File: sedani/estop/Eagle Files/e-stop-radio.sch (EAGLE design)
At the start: 33 parts, among them J1 E-STOP HEADER, J2 AVR_SPI_PROG_3X2PTH, J3 Buttons, U1 RFM69HCW, U2 TPS62203DBVR, U3 CD40109BPWRPW16-L, X1 8 MHz

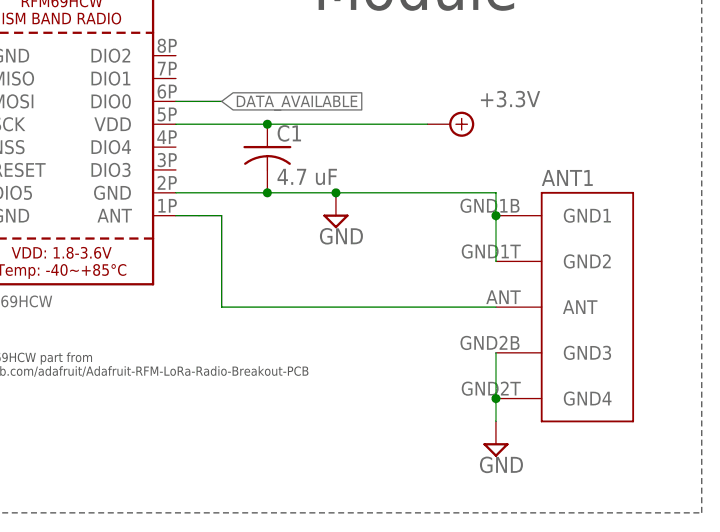
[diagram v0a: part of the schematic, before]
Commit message: changed antenna part
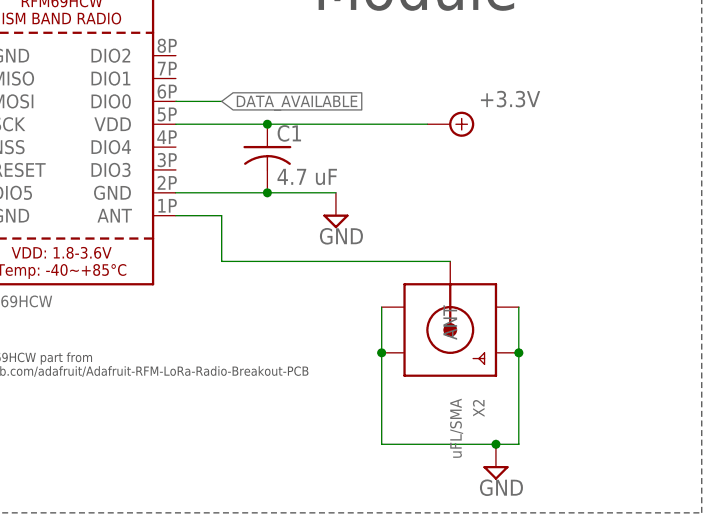
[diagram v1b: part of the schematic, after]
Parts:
- removed ANT1: (no value), estop-v1.0:CON-SMA-EDGE-S
- added X2: uFL/SMA, microbuilder:SMACONNECTOR_EDGE_UFL
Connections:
- net GND: now also X2.GND1, X2.GND2, X2.GND3, X2.GND4; no longer ANT1.GND1, ANT1.GND2, ANT1.GND3, ANT1.GND4
- net RF_SIGNAL: now also X2.ANT; no longer ANT1.ANT
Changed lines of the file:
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@@
 <part name="C5" library="rcl" library_urn="urn:adsk.eagle:library:334" deviceset="C-US" device="C0603" package3d_urn="urn:adsk.eagle:package:23616/2" value="4.7uF"/>
 <part name="C7" library="rcl" library_urn="urn:adsk.eagle:library:334" deviceset="CPOL-US" device="E2.5-7" package3d_urn="urn:adsk.eagle:package:23345/1" value="220uF"/>
-<part name="ANT1" library="estop-v1.0" deviceset="CON-SMA-EDGE-S" device=""/>
 <part name="SUPPLY20" library="supply2" library_urn="urn:adsk.eagle:library:372" deviceset="GND" device=""/>
+<part name="X2" library="microbuilder" deviceset="SMACONNECTOR" device="_EDGE_UFL" value="uFL/SMA"/>
 </parts>
 <sheets>
@@
 <attribute name="VALUE" x="255.016" y="-27.051" size="1.778" layer="96"/>
 </instance>
-<instance part="ANT1" gate="G$1" x="358.14" y="-30.48" smashed="yes">
-<attribute name="VALUE" x="358.14" y="-45.72" size="1.778" layer="95" font="vector"/>
-<attribute name="NAME" x="358.14" y="-15.24" size="1.778" layer="95" font="vector" align="top-left"/>
-</instance>
-<instance part="SUPPLY20" gate="GND" x="353.06" y="-45.72" smashed="yes">
-<attribute name="VALUE" x="351.155" y="-48.895" size="1.778" layer="96"/>
+<instance part="SUPPLY20" gate="GND" x="353.06" y="-48.26" smashed="yes">
+<attribute name="VALUE" x="351.155" y="-51.435" size="1.778" layer="96"/>
+</instance>
+<instance part="X2" gate="G$1" x="347.98" y="-33.02" smashed="yes" rot="R270">
+<attribute name="NAME" x="350.52" y="-40.64" size="1.27" layer="95" rot="R270"/>
+<attribute name="VALUE" x="347.98" y="-40.64" size="1.27" layer="95" rot="R270"/>
 </instance>
 </instances>
@@
 <wire x1="327.66" y1="-17.78" x2="335.28" y2="-17.78" width="0.1524" layer="91"/>
 <junction x="327.66" y="-17.78"/>
-<wire x1="335.28" y1="-17.78" x2="353.06" y2="-17.78" width="0.1524" layer="91"/>
-<junction x="335.28" y="-17.78"/>
-<pinref part="ANT1" gate="G$1" pin="GND2"/>
-<wire x1="353.06" y1="-17.78" x2="353.06" y2="-20.32" width="0.1524" layer="91"/>
-<pinref part="ANT1" gate="G$1" pin="GND1"/>
-<wire x1="353.06" y1="-20.32" x2="353.06" y2="-25.4" width="0.1524" layer="91"/>
-<junction x="353.06" y="-20.32"/>
 </segment>
 <segment>
@@
 </segment>
 <segment>
+<pinref part="X2" gate="G$1" pin="GND1"/>
+<pinref part="X2" gate="G$1" pin="GND2"/>
+<wire x1="355.6" y1="-30.48" x2="355.6" y2="-35.56" width="0.1524" layer="91"/>
 <pinref part="SUPPLY20" gate="GND" pin="GND"/>
-<pinref part="ANT1" gate="G$1" pin="GND4"/>
-<wire x1="353.06" y1="-43.18" x2="353.06" y2="-40.64" width="0.1524" layer="91"/>
-<pinref part="ANT1" gate="G$1" pin="GND3"/>
-<wire x1="353.06" y1="-40.64" x2="353.06" y2="-35.56" width="0.1524" layer="91"/>
-<junction x="353.06" y="-40.64"/>
+<wire x1="355.6" y1="-35.56" x2="355.6" y2="-45.72" width="0.1524" layer="91"/>
+<wire x1="355.6" y1="-45.72" x2="353.06" y2="-45.72" width="0.1524" layer="91"/>
+<junction x="355.6" y="-35.56"/>
+<pinref part="X2" gate="G$1" pin="GND3"/>
+<pinref part="X2" gate="G$1" pin="GND4"/>
+<wire x1="340.36" y1="-30.48" x2="340.36" y2="-35.56" width="0.1524" layer="91"/>
+<wire x1="340.36" y1="-35.56" x2="340.36" y2="-45.72" width="0.1524" layer="91"/>
+<wire x1="340.36" y1="-45.72" x2="353.06" y2="-45.72" width="0.1524" layer="91"/>
+<junction x="340.36" y="-35.56"/>
+<junction x="353.06" y="-45.72"/>
 </segment>
 </net>
@@
 <net name="RF_SIGNAL" class="2">
 <segment>
-<pinref part="ANT1" gate="G$1" pin="ANT"/>
-<wire x1="322.58" y1="-30.48" x2="353.06" y2="-30.48" width="0.1524" layer="91"/>
 <pinref part="U1" gate="G$1" pin="ANT"/>
-<wire x1="317.5" y1="-20.32" x2="320.04" y2="-20.32" width="0.1524" layer="91"/>
-<wire x1="322.58" y1="-30.48" x2="322.58" y2="-20.32" width="0.1524" layer="91"/>
-<wire x1="322.58" y1="-20.32" x2="320.04" y2="-20.32" width="0.1524" layer="91"/>
-</segment>
-</net>
+<wire x1="322.58" y1="-20.32" x2="317.5" y2="-20.32" width="0.1524" layer="91"/>
+<pinref part="X2" gate="G$1" pin="ANT"/>
+<wire x1="347.98" y1="-25.4" x2="322.58" y2="-25.4" width="0.1524" layer="91"/>
+<wire x1="322.58" y1="-25.4" x2="322.58" y2="-20.32" width="0.1524" layer="91"/>
+</segment>
+</net>

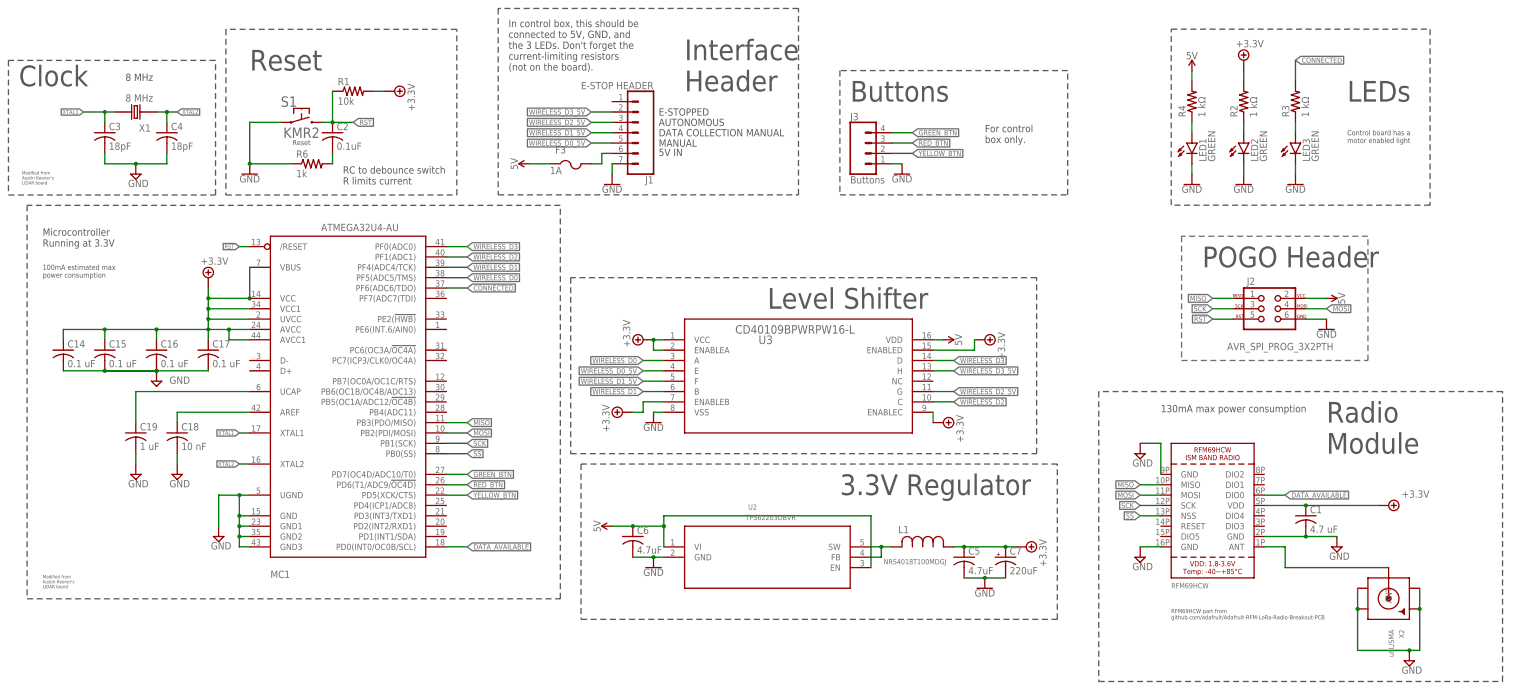
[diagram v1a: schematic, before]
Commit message: fixed library parts and generated board
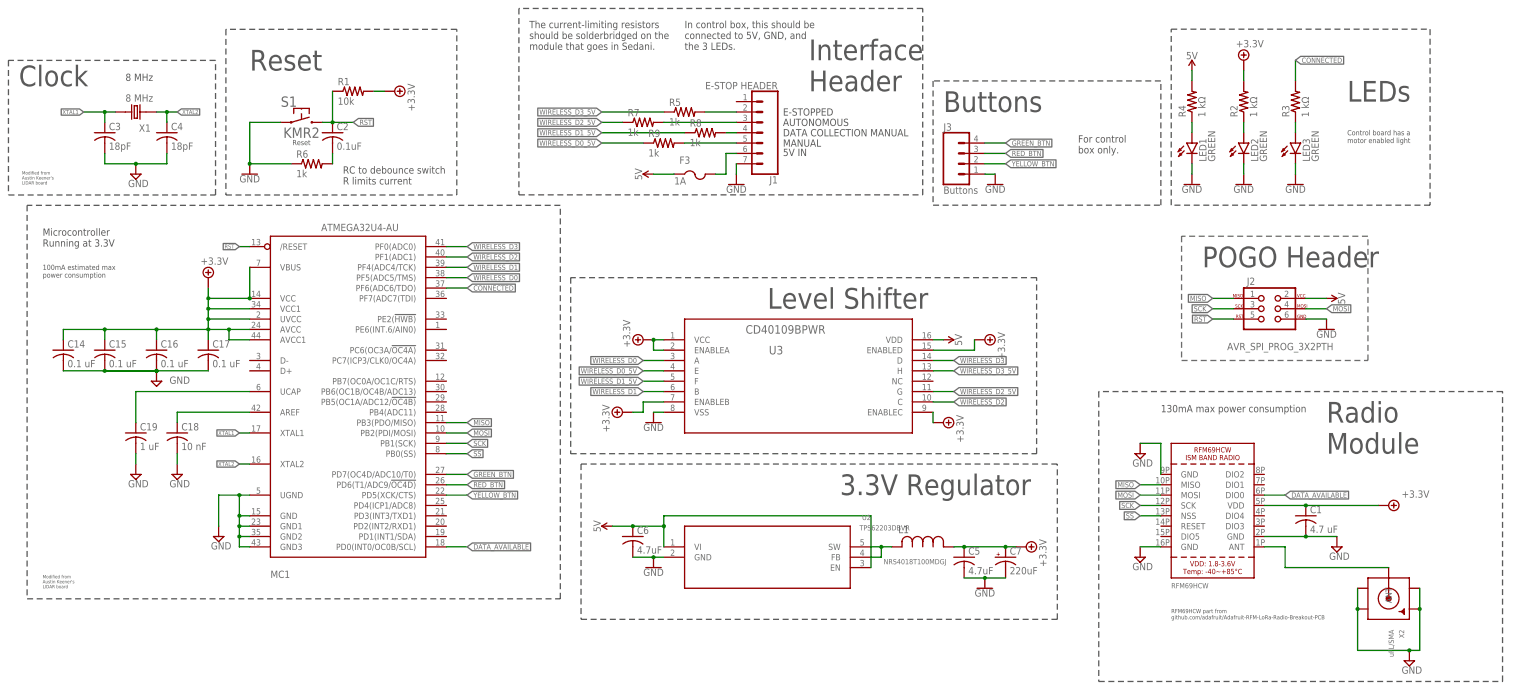
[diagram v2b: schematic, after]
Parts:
- added R5, R7, R8, R9: 1k, rcl:R-US_R0603
- U3: value CD40109BPWRPW16-L -> CD40109BPWR; device estop-v1.0:CD40109BPWRPW16-L -> estop-v1.0:CD40109BPWR
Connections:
- new net N$10: J1.3, R7.2
- new net N$6: J1.4, R8.2
- new net N$8: J1.5, R9.2
- new net N$9: J1.2, R5.2
- net WIRELESS_D0_5V: now also R9.1; no longer J1.5
- net WIRELESS_D1_5V: now also R8.1; no longer J1.4
- net WIRELESS_D2_5V: now also R7.1; no longer J1.3
- net WIRELESS_D3_5V: now also R5.1; no longer J1.2
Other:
- note added: "In control box, this should be connected to 5V, GND, and the 3 LEDs."
- note added: "The current-limiting resistors should be solderbridged on the module that goes in Sedani."
- note removed: "In control box, this should be connected to 5V, GND, and the 3 LEDs. Don't forget the current-limiting resistors (not on the board)."
- moved on the sheet: F3, J1, J3

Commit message: major parts on board
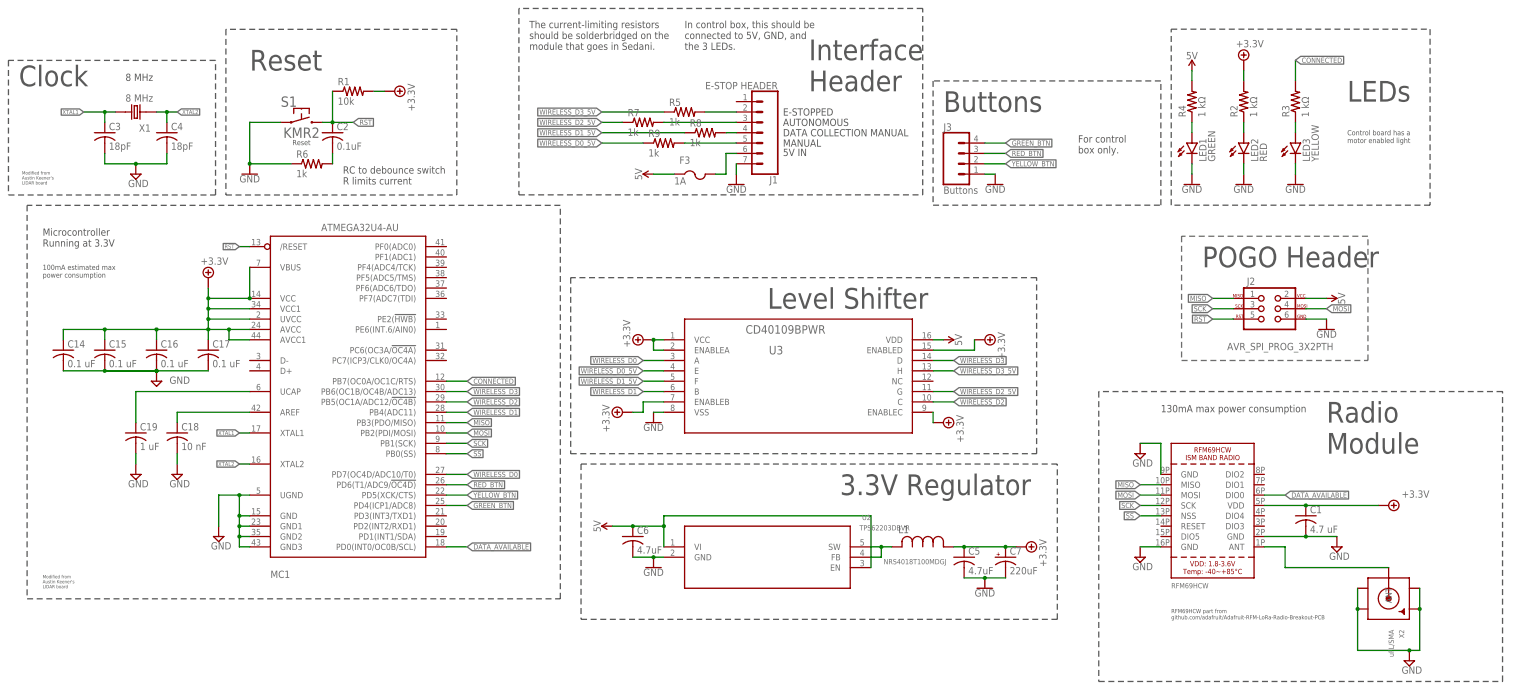
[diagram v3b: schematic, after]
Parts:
- LED2: value GREEN -> RED
- LED3: value GREEN -> YELLOW
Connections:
- net CONNECTED: now also MC1.PB7(OC0A/OC1C/RTS); no longer MC1.PF6(ADC6/TDO)
- net GREEN_BTN: now also MC1.PD4(ICP1/ADC8); no longer MC1.PD7(OC4D/ADC10/T0)
- net WIRELESS_D0: now also MC1.PD7(OC4D/ADC10/T0); no longer MC1.PF5(ADC5/TMS)
- net WIRELESS_D1: now also MC1.PB4(ADC11); no longer MC1.PF4(ADC4/TCK)
- net WIRELESS_D2: now also MC1.PB5(OC1A/ADC12/!OC4B); no longer MC1.PF1(ADC1)
- net WIRELESS_D3: now also MC1.PB6(OC1B/OC4B/ADC13); no longer MC1.PF0(ADC0)
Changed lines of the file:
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@@
 <part name="R4" library="rcl" library_urn="urn:adsk.eagle:library:334" deviceset="R-US_" device="R0603" package3d_urn="urn:adsk.eagle:package:23555/3" value="1 kΩ"/>
 <part name="GND5" library="SparkFun-PowerSymbols" deviceset="GND" device=""/>
-<part name="LED2" library="led" library_urn="urn:adsk.eagle:library:259" deviceset="LED" device="CHIP-LED0603" package3d_urn="urn:adsk.eagle:package:15819/3" value="GREEN"/>
+<part name="LED2" library="led" library_urn="urn:adsk.eagle:library:259" deviceset="LED" device="CHIP-LED0603" package3d_urn="urn:adsk.eagle:package:15819/3" value="RED"/>
 <part name="R2" library="rcl" library_urn="urn:adsk.eagle:library:334" deviceset="R-US_" device="R0603" package3d_urn="urn:adsk.eagle:package:23555/3" value="1 kΩ"/>
 <part name="GND6" library="SparkFun-PowerSymbols" deviceset="GND" device=""/>
-<part name="LED3" library="led" library_urn="urn:adsk.eagle:library:259" deviceset="LED" device="CHIP-LED0603" package3d_urn="urn:adsk.eagle:package:15819/3" value="GREEN"/>
+<part name="LED3" library="led" library_urn="urn:adsk.eagle:library:259" deviceset="LED" device="CHIP-LED0603" package3d_urn="urn:adsk.eagle:package:15819/3" value="YELLOW"/>
 <part name="R3" library="rcl" library_urn="urn:adsk.eagle:library:334" deviceset="R-US_" device="R0603" package3d_urn="urn:adsk.eagle:package:23555/3" value="1 kΩ"/>
 <part name="GND7" library="SparkFun-PowerSymbols" deviceset="GND" device=""/>
@@
 <net name="WIRELESS_D3" class="0">
 <segment>
-<pinref part="MC1" gate="G$1" pin="PF0(ADC0)"/>
-<wire x1="116.84" y1="53.34" x2="121.92" y2="53.34" width="0.1524" layer="91"/>
-<label x="121.92" y="53.34" size="1.27" layer="95" font="vector" xref="yes"/>
-</segment>
-<segment>
 <wire x1="236.22" y1="25.4" x2="241.3" y2="25.4" width="0.1524" layer="91"/>
 <label x="241.3" y="25.4" size="1.27" layer="95" font="vector" xref="yes"/>
 <pinref part="U3" gate="A" pin="D"/>
 </segment>
+<segment>
+<wire x1="116.84" y1="17.78" x2="121.92" y2="17.78" width="0.1524" layer="91"/>
+<label x="121.92" y="17.78" size="1.27" layer="95" font="vector" xref="yes"/>
+<pinref part="MC1" gate="G$1" pin="PB6(OC1B/OC4B/ADC13)"/>
+</segment>
 </net>
 <net name="WIRELESS_D2" class="0">
-<segment>
-<pinref part="MC1" gate="G$1" pin="PF1(ADC1)"/>
-<wire x1="116.84" y1="50.8" x2="121.92" y2="50.8" width="0.1524" layer="91"/>
-<label x="121.92" y="50.8" size="1.27" layer="95" font="vector" xref="yes"/>
-</segment>
 <segment>
 <wire x1="236.22" y1="15.24" x2="241.3" y2="15.24" width="0.1524" layer="91"/>
@@
 <pinref part="U3" gate="A" pin="C"/>
 </segment>
+<segment>
+<wire x1="116.84" y1="15.24" x2="121.92" y2="15.24" width="0.1524" layer="91"/>
+<label x="121.92" y="15.24" size="1.27" layer="95" font="vector" xref="yes"/>
+<pinref part="MC1" gate="G$1" pin="PB5(OC1A/ADC12/!OC4B)"/>
+</segment>
 </net>
 <net name="WIRELESS_D1" class="0">
-<segment>
-<pinref part="MC1" gate="G$1" pin="PF4(ADC4/TCK)"/>
-<wire x1="116.84" y1="48.26" x2="121.92" y2="48.26" width="0.1524" layer="91"/>
-<label x="121.92" y="48.26" size="1.27" layer="95" font="vector" xref="yes"/>
-</segment>
 <segment>
 <wire x1="170.18" y1="17.78" x2="165.1" y2="17.78" width="0.1524" layer="91"/>
@@
 <pinref part="U3" gate="A" pin="B"/>
 </segment>
+<segment>
+<wire x1="116.84" y1="12.7" x2="121.92" y2="12.7" width="0.1524" layer="91"/>
+<label x="121.92" y="12.7" size="1.27" layer="95" font="vector" xref="yes"/>
+<pinref part="MC1" gate="G$1" pin="PB4(ADC11)"/>
+</segment>
 </net>
 <net name="WIRELESS_D0" class="0">
-<segment>
-<pinref part="MC1" gate="G$1" pin="PF5(ADC5/TMS)"/>
-<wire x1="116.84" y1="45.72" x2="121.92" y2="45.72" width="0.1524" layer="91"/>
-<label x="121.92" y="45.72" size="1.27" layer="95" font="vector" xref="yes"/>
-</segment>
 <segment>
 <wire x1="170.18" y1="25.4" x2="165.1" y2="25.4" width="0.1524" layer="91"/>
 <label x="165.1" y="25.4" size="1.27" layer="95" font="vector" rot="MR0" xref="yes"/>
 <pinref part="U3" gate="A" pin="A"/>
+</segment>
+<segment>
+<wire x1="116.84" y1="-2.54" x2="121.92" y2="-2.54" width="0.1524" layer="91"/>
+<label x="121.92" y="-2.54" size="1.27" layer="95" font="vector" xref="yes"/>
+<pinref part="MC1" gate="G$1" pin="PD7(OC4D/ADC10/T0)"/>
 </segment>
 </net>
@@
 <net name="CONNECTED" class="0">
 <segment>
-<pinref part="MC1" gate="G$1" pin="PF6(ADC6/TDO)"/>
-<wire x1="116.84" y1="43.18" x2="121.92" y2="43.18" width="0.1524" layer="91"/>
-<label x="121.92" y="43.18" size="1.27" layer="95" font="vector" xref="yes"/>
-</segment>
-<segment>
 <pinref part="R3" gate="G$1" pin="2"/>
 <wire x1="325.12" y1="93.98" x2="325.12" y2="99.06" width="0.1524" layer="91"/>
 <label x="325.12" y="99.06" size="1.27" layer="95" font="vector" xref="yes"/>
 </segment>
+<segment>
+<wire x1="116.84" y1="20.32" x2="121.92" y2="20.32" width="0.1524" layer="91"/>
+<label x="121.92" y="20.32" size="1.27" layer="95" font="vector" xref="yes"/>
+<pinref part="MC1" gate="G$1" pin="PB7(OC0A/OC1C/RTS)"/>
+</segment>
 </net>
 <net name="WIRELESS_D3_5V" class="0">
@@
 </segment>
 <segment>
-<wire x1="116.84" y1="-2.54" x2="121.92" y2="-2.54" width="0.1524" layer="91"/>
-<label x="121.92" y="-2.54" size="1.27" layer="95" font="vector" xref="yes"/>
-<pinref part="MC1" gate="G$1" pin="PD7(OC4D/ADC10/T0)"/>
-</segment>
-</net>
+<wire x1="116.84" y1="-10.16" x2="121.92" y2="-10.16" width="0.1524" layer="91"/>
+<label x="121.92" y="-10.16" size="1.27" layer="95" font="vector" xref="yes"/>
+<pinref part="MC1" gate="G$1" pin="PD4(ICP1/ADC8)"/>
+</segment>
+</net>
